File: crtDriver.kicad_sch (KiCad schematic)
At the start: 30 parts, among them J1 Lum_In, J2 V_Sync, J3 H_Sync, Q1 2N7000, Q2 2N7000, Q3 2N7000, Q4 2N7000

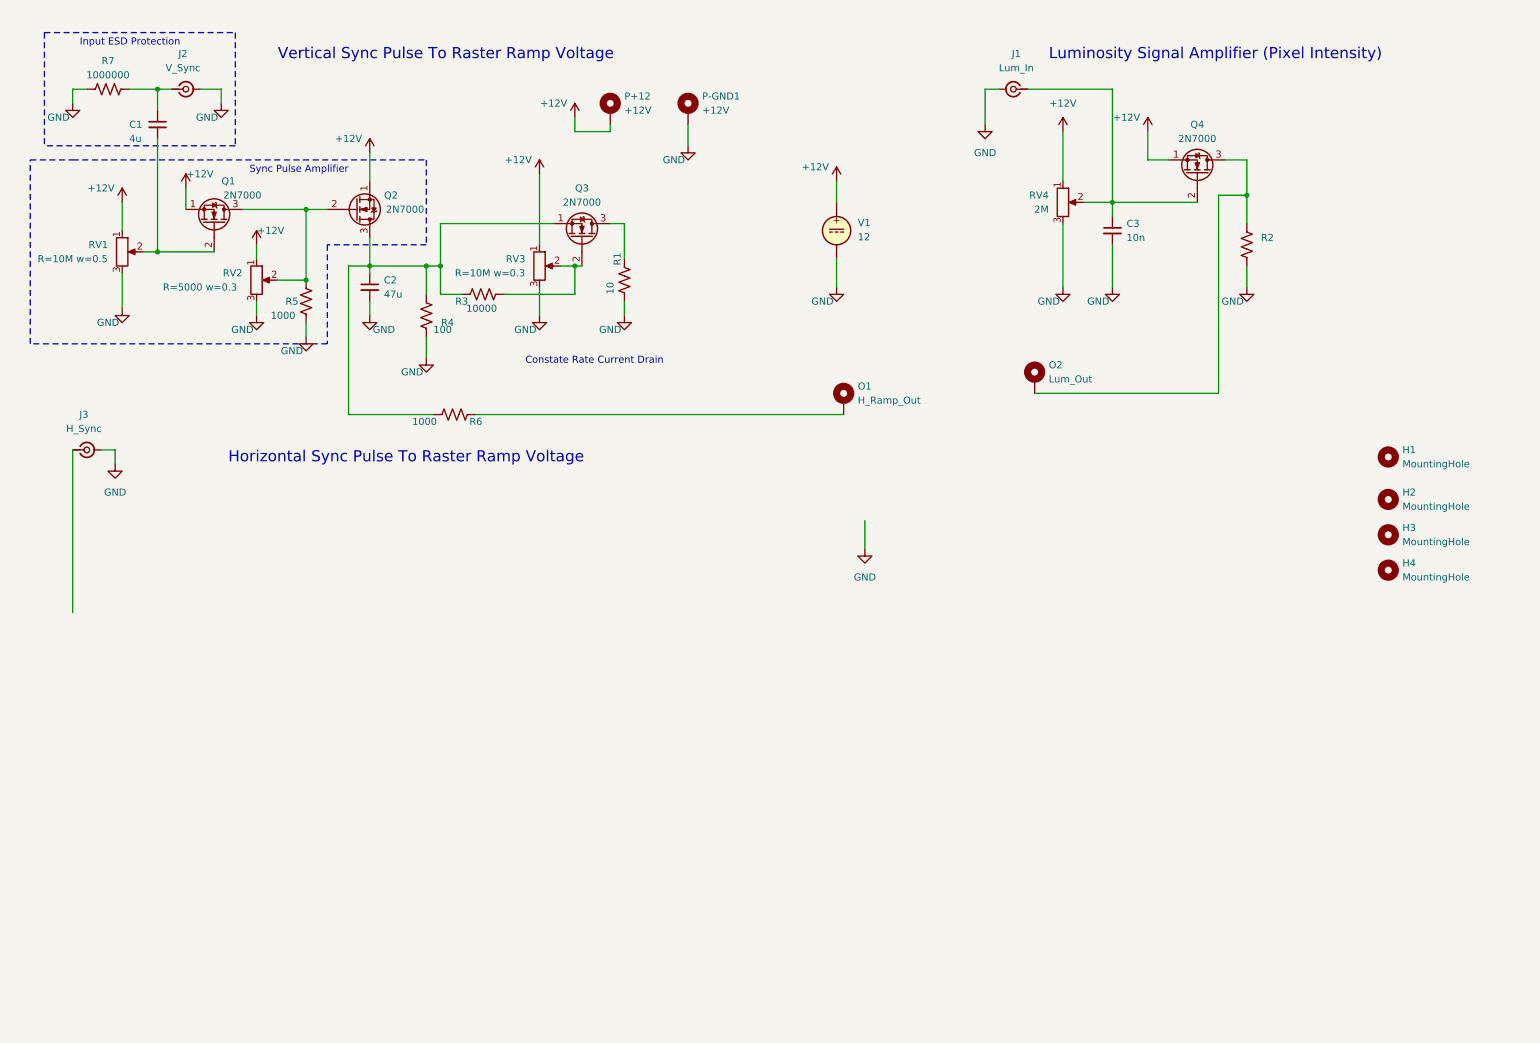
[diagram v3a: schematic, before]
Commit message: changed circuit to use 2n7000's as low side switches/valves to get voltage gain, started on current mirror for linear capacitor voltage ramp (it also will likely only work on the low side maybe requiring inverting of the fill/drain modes/roles, fixed luminosity amplifier design by also using mosfet on low(-) side of a resistor to boost the voltage of the input signal
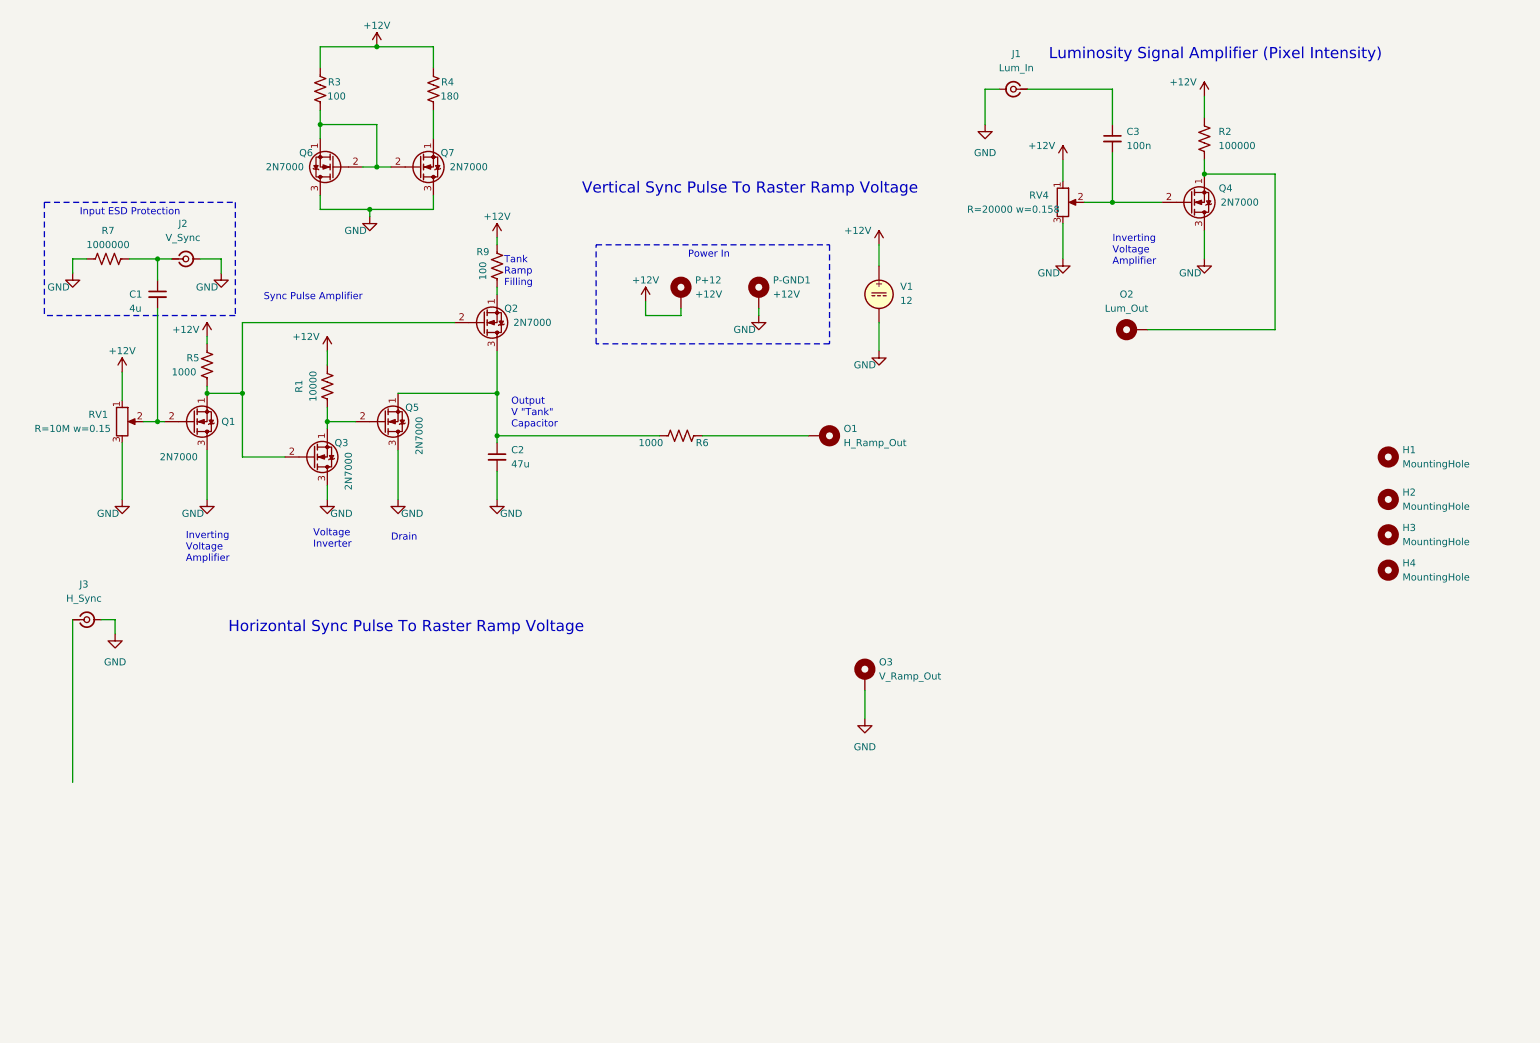
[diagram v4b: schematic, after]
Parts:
- removed RV2: 2M, crtDriver:Potentiometer_Triwood_RM-065, symbol Device:R_Potentiometer
- removed RV3: 10M, crtDriver:Potentiometer_Triwood_RM-065, symbol Device:R_Potentiometer
- added O3: V_Ramp_Out, Connector_Wire:SolderWire-0.25sqmm_1x01_D0.65mm_OD2mm_Relief, symbol Mechanical:MountingHole_Pad
- added Q5, Q6, Q7: 2N7000, Package_TO_SOT_THT:TO-92_Inline, symbol Transistor_FET:2N7000
- added R9: 100, Resistor_SMD:R_0603_1608Metric, symbol Device:R_US
- C3: value 10n -> 100n
- R1: value 10 -> 10000; footprint Resistor_SMD:R_1210_3225Metric -> Resistor_SMD:R_0603_1608Metric
- R2: value 1000 -> 100000
- R3: value 10000 -> 100
- R4: value 100 -> 180; footprint Resistor_SMD:R_1210_3225Metric -> Resistor_SMD:R_0603_1608Metric
- R5: footprint Resistor_SMD:R_0805_2012Metric -> Resistor_SMD:R_1210_3225Metric
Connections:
- net +12V: now also R1.1, R2.1, R3.1, R4.1, R5.1, R9.1; no longer Q1.1 (S), Q2.1 (S), Q4.1 (S)
- net GND: now also Q1.3 (D), Q3.3 (D), Q4.3 (D), O3.1, Q5.3 (D), Q6.3 (D), Q7.3 (D); no longer C3.2, R1.2, R2.2, R4.2, R5.2
- net at C2.1, Q2.3 (D), R6.2: now also Q5.1 (S); no longer Q3.1 (S), R3.1, R4.1
- net at R3.2: now also Q6.1 (S), Q6.2 (G), Q7.2 (G); no longer Q3.2 (G)
- net at Q4.2 (G), RV4.2: now also C3.2; no longer C3.1, J1.1 (In)
- new net: O2.1, Q4.1 (S), R2.2
- new net: Q7.1 (S), R4.2
- new net: C3.1, J1.1 (In)
- new net: Q3.1 (S), Q5.2 (G), R1.2
- new net: Q1.1 (S), Q2.2 (G), Q3.2 (G), R5.2
- new net: Q2.1 (S), R9.2
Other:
- note added: "Drain"
- note added: "Inverting Voltage Amplifier"
- note added: "Output V "Tank" Capacitor"
- note added: "Power In"
- note added: "Tank Ramp Filling"
- note added: "Voltage Inverter"
- note removed: "Constate Rate Current Drain"
- moved on the sheet: C1, C2, C3, J2, J3, O1, O2, P+12, P-GND1, Q1, Q4, R2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

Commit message: changed design to have a current mirror constant current drain for output capacitor and added components to improve performance of it
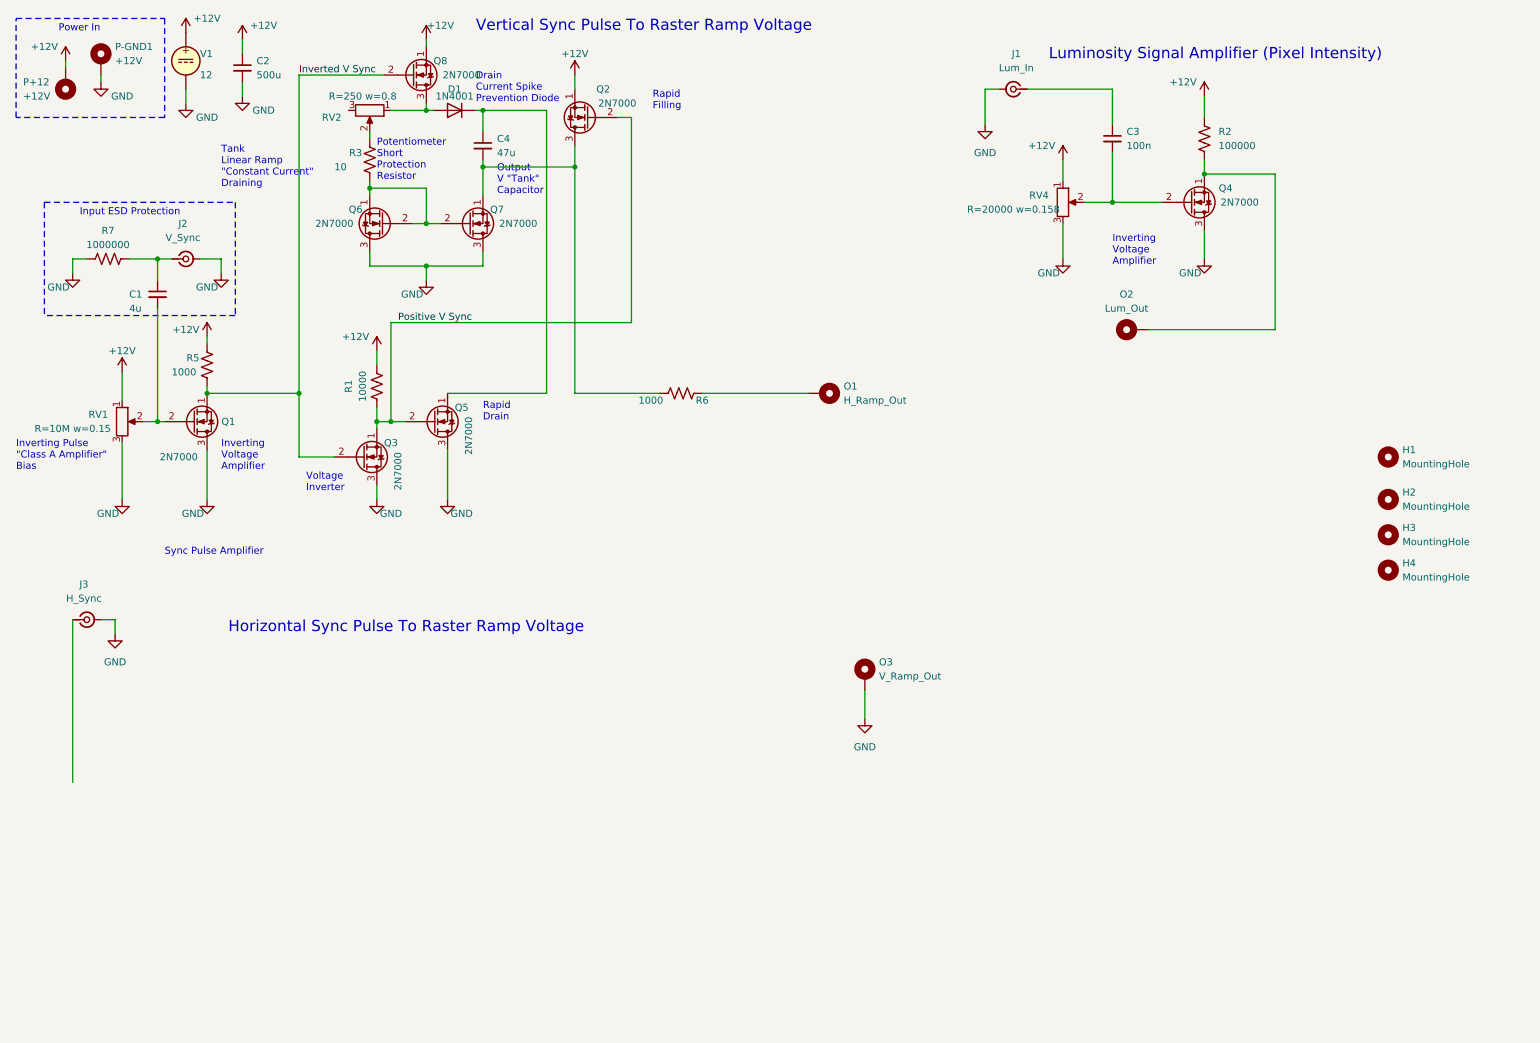
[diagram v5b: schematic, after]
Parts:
- removed R4: 180, Resistor_SMD:R_0603_1608Metric, symbol Device:R_US
- removed R9: 100, Resistor_SMD:R_0603_1608Metric, symbol Device:R_US
- added C4: 47u, Capacitor_SMD:C_1206_3216Metric, symbol Device:C_Small
- added D1: 1N4001, Diode_THT:D_DO-41_SOD81_P10.16mm_Horizontal, symbol Diode:1N4001
- added Q8: 2N7000, Package_TO_SOT_THT:TO-92_Inline, symbol Transistor_FET:2N7000
- added RV2: 250, crtDriver:Potentiometer_Triwood_RM-065, symbol Device:R_Potentiometer
- C2: value 47u -> 500u
- R3: value 100 -> 10; footprint Resistor_SMD:R_0603_1608Metric -> Resistor_SMD:R_1210_3225Metric
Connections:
- net +12V: now also C2.1, Q2.1 (S), Q8.1 (S); no longer R3.1
- net at Q2.3 (D), R6.2: now also Q7.1 (S), C4.2; no longer C2.1, Q5.1 (S)
- net Positive V Sync: now reaches Q3.1 (S), Q5.2 (G), R1.2
- net Positive V Sync: now also Q2.2 (G)
- net Inverted V Sync: now reaches Q1.1 (S), Q3.2 (G), R5.2
- net Inverted V Sync: now also Q8.2 (G); no longer Q2.2 (G)
- new net: R3.1, RV2.2
- new net: C4.1, D1.1 (K), Q5.1 (S)
- new net: D1.2 (A), Q8.3 (D), RV2.1
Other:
- note added: "Drain Current Spike Prevention Diode"
- note added: "Inverting Pulse "Class A Amplifier" Bias"
- note added: "Potentiometer Short Protection Resistor"
- note added: "Rapid Drain"
- note added: "Rapid Filling"
- note added: "Tank Linear Ramp "Constant Current" Draining"
- note removed: "Drain"
- note removed: "Tank Ramp Filling"
- moved on the sheet: O1, P+12, P-GND1, Q3, Q5, Q6, Q7, R1, R6, V1

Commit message: duplicated v sync section for h sync, adjusted luminosity amplifier passive component values
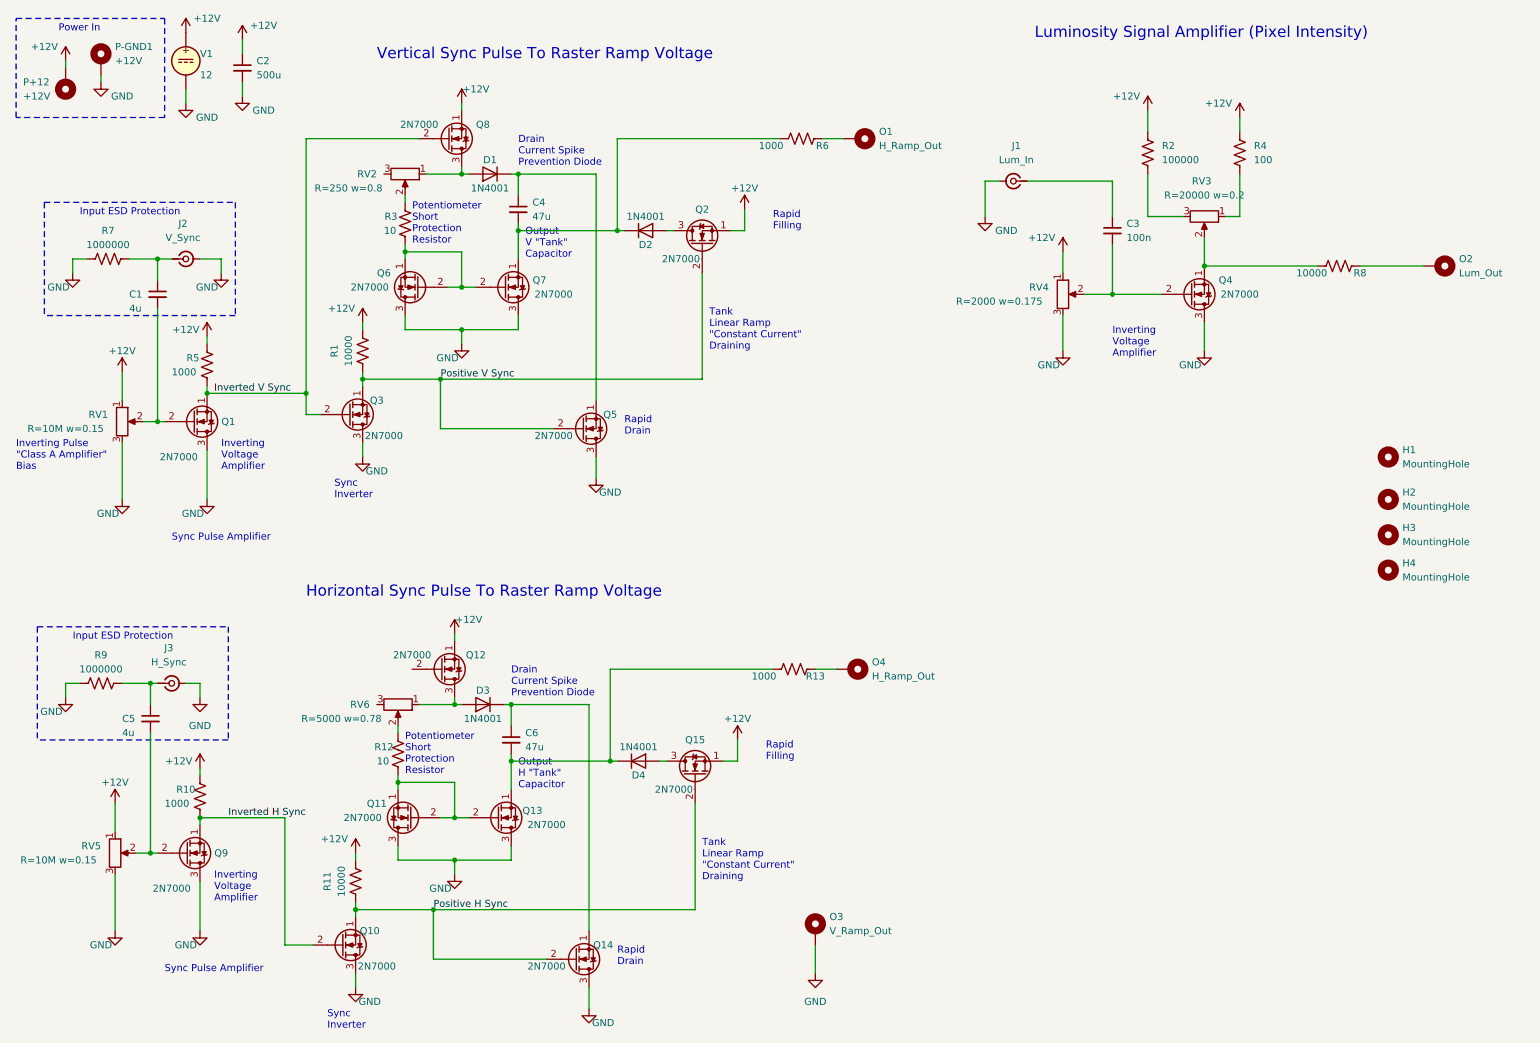
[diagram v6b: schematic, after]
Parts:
- added C5: 4u, Capacitor_SMD:C_0603_1608Metric, symbol Device:C_Small
- added C6: 47u, Capacitor_SMD:C_1206_3216Metric, symbol Device:C_Small
- added D2, D3, D4: 1N4001, Diode_THT:D_DO-41_SOD81_P10.16mm_Horizontal, symbol Diode:1N4001
- added O4: H_Ramp_Out, Connector_Wire:SolderWire-0.25sqmm_1x01_D0.65mm_OD2mm_Relief, symbol Mechanical:MountingHole_Pad
- added Q10, Q11, Q12, Q13, Q14, Q15, Q9: 2N7000, Package_TO_SOT_THT:TO-92_Inline, symbol Transistor_FET:2N7000
- added R10: 1000, Resistor_SMD:R_1210_3225Metric, symbol Device:R_US
- added R11, R8: 10000, Resistor_SMD:R_0603_1608Metric, symbol Device:R_US
- added R12: 10, Resistor_SMD:R_1210_3225Metric, symbol Device:R_US
- added R13: 1000, Resistor_SMD:R_0603_1608Metric, symbol Device:R_US
- added R4: 100, Resistor_SMD:R_0805_2012Metric, symbol Device:R_US
- added R9: 1000000, Resistor_SMD:R_0603_1608Metric, symbol Device:R_US
- added RV3: 2000, crtDriver:Potentiometer_Triwood_RM-065, symbol Device:R_Potentiometer
- added RV5: 2M, crtDriver:Potentiometer_Triwood_RM-065, symbol Device:R_Potentiometer
- added RV6: 5000, crtDriver:Potentiometer_Triwood_RM-065, symbol Device:R_Potentiometer
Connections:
- net +12V: now also Q12.1 (S), Q15.1 (S), R10.1, R11.1, R4.1, RV5.1
- net GND: now also Q10.3 (D), Q11.3 (D), Q13.3 (D), Q14.3 (D), Q9.3 (D), R9.2, RV5.3
- net at C4.2, Q7.1 (S), R6.2: now also D2.1 (K); no longer Q2.3 (D)
- net at J3.1 (In): now also C5.1, R9.1
- new net: O4.1, R13.1
- new net: Q4.1 (S), R8.2, RV3.2
- new net: C6.1, D3.1 (K), Q14.1 (S)
- new net: C5.2, Q9.2 (G), RV5.2
- new net: R2.2, RV3.3
- new net: C6.2, D4.1 (K), Q13.1 (S), R13.2
- new net: Q11.1 (S), Q11.2 (G), Q13.2 (G), R12.2
- new net: O2.1, R8.1
- new net: D3.2 (A), Q12.3 (D), RV6.1
- new net: R12.1, RV6.2
- new net: R4.2, RV3.1
- new net: D4.2 (A), Q15.3 (D)
- new net: D2.2 (A), Q2.3 (D)
- new net Inverted H Sync: Q10.2 (G), Q9.1 (S), R10.2
- new net Positive H Sync: Q10.1 (S), Q14.2 (G), Q15.2 (G), R11.2
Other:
- note added: "Output H "Tank" Capacitor"
- note added: "Sync Inverter"
- note removed: "Voltage Inverter"
- moved on the sheet: C3, C4, D1, J1, J3, O1, O2, O3, Q2, Q3, Q4, Q5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

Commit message: updated schematic with voltage booster section, haven't found settings for it to be simulated stabily in spice without many iterations/timesteps yet
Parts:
- removed D1, D2, D3, D4: 1N4001, Diode_THT:D_DO-41_SOD81_P10.16mm_Horizontal, symbol Diode:1N4001
- removed O3: V_Ramp_Out, Connector_Wire:SolderWire-0.25sqmm_1x01_D0.65mm_OD2mm_Relief, symbol Mechanical:MountingHole_Pad
- added C7: 20u, Capacitor_SMD:C_0603_1608Metric, symbol Device:C
- added C9: 500u, Capacitor_SMD:C_1206_3216Metric, symbol Device:C_Small
- added D1, D2, D3, D4, D5, D6, D7: US1A, Diode_SMD:D_SMA, symbol Diode:US1A
- added Q16, Q17: 2N7000, Package_TO_SOT_SMD:SOT-23, symbol Transistor_FET:2N7000
- added R14: 100000, Resistor_SMD:R_0603_1608Metric, symbol Device:R_US
- added R15: .5, Resistor_SMD:R_1210_3225Metric, symbol Device:R_US
- added R16, R17: 1, Resistor_SMD:R_0603_1608Metric, symbol Device:R_US
- added RV10, RV7, RV8: 2000, Potentiometer_SMD:Potentiometer_Bourns_TC33X_Vertical, symbol Device:R_Potentiometer
- added T1: Transformer_1P_1S, Transformer_SMD:Transformer_Wuerth_750315371, symbol Device:Transformer_1P_1S
- J2: value V_Sync -> H_Sync
- J3: value H_Sync -> V_Sync
- O4: value H_Ramp_Out -> V_Ramp_Out
- Q1, Q10, Q11, Q12, Q13, Q14, Q15, Q2, Q3, Q4, Q5, Q6, Q7, Q8, Q9: footprint Package_TO_SOT_THT:TO-92_Inline -> Package_TO_SOT_SMD:SOT-23
- RV1, RV2, RV3, RV4, RV5, RV6: footprint crtDriver:Potentiometer_Triwood_RM-065 -> Potentiometer_SMD:Potentiometer_Bourns_TC33X_Vertical
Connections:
- net +12V: now also C9.1, D7.1 (K), R15.2, RV10.1, T1.1 (AA); no longer V1.1
- net GND: now also C7.2, C9.2, Q17.3 (D), R14.2, R16.2, R17.2, RV10.3, RV8.3
- net Inverted H Sync: now also Q1.1 (S), Q3.2 (G), Q8.2 (G), R5.2; no longer Q10.2 (G), Q9.1 (S), R10.2
- net Inverted V Sync: now also Q10.2 (G), Q12.2 (G), Q9.1 (S), R10.2; no longer Q1.1 (S), Q3.2 (G), Q8.2 (G), R5.2
- net Positive H Sync: now also Q2.2 (G), Q3.1 (S), Q5.2 (G), R1.2; no longer Q10.1 (S), Q14.2 (G), Q15.2 (G), R11.2
- net Positive V Sync: now also Q10.1 (S), Q14.2 (G), Q15.2 (G), R11.2; no longer Q2.2 (G), Q3.1 (S), Q5.2 (G), R1.2
- net at C4.1, Q5.1 (S): now also D6.1 (K)
- net at Q8.3 (D), RV2.1: now also D6.2 (A)
- net at C4.2, Q7.1 (S), R6.2: now also D1.1 (K), RV7.1
- net at C6.1, Q14.1 (S): now also D2.1 (K)
- net at C6.2, Q13.1 (S), R13.2: now also D3.1 (K)
- net at Q12.3 (D), RV6.1: now also D2.2 (A)
- net at Q15.3 (D): now also D3.2 (A)
- net at Q2.3 (D): now also D1.2 (A)
- new net: D4.2 (A), D5.1 (K), T1.4 (SB)
- new net: D5.2 (A), R17.1, T1.3 (SA)
- new net: C7.1, D4.1 (K), R14.1
- new net: D7.2 (A), Q16.1 (S), T1.2 (AB)
- new net: Q16.2 (G), Q17.1 (S), RV10.2, RV8.1
- new net: Q16.3 (D), R16.1
- new net: R15.1, V1.1
- new net: Q17.2 (G), RV7.2
- new net: RV7.3, RV8.2
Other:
- note added: ".OPTIONS ITL4=100 .OPTIONS RELTOL=0.003 .tran 1n 100m"
- note added: "Horizontal Ramp Driven High Voltage Flyback Transformer"
- note added: "Ramp Inverter"
- moved on the sheet: C2, H1, H2, H3, H4, V1
